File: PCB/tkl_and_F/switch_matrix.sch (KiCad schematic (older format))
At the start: 214 parts

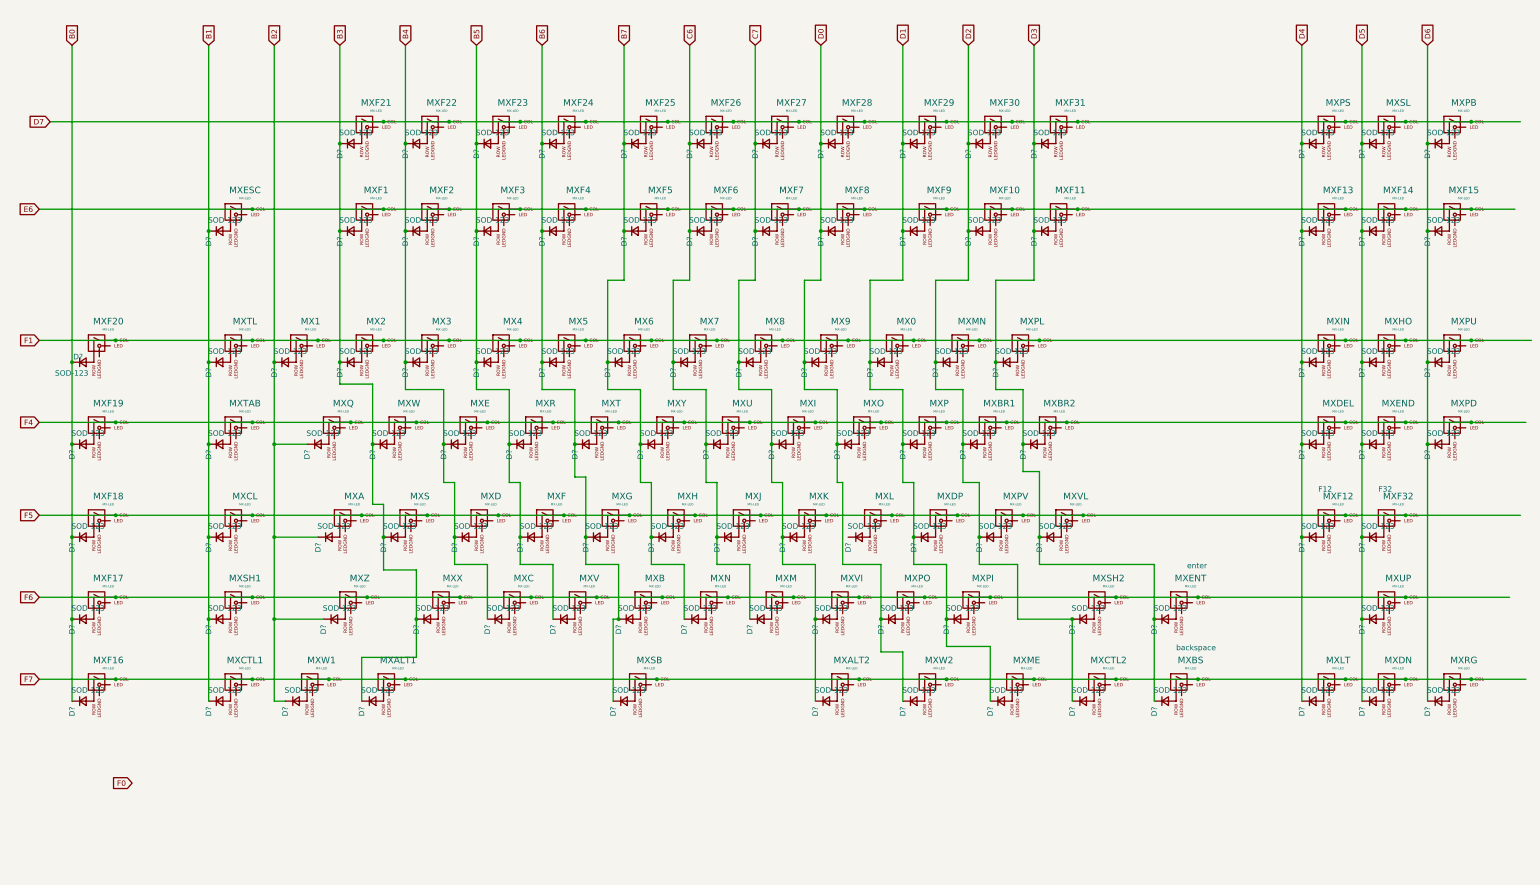
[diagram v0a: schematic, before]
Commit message: footprint assigment
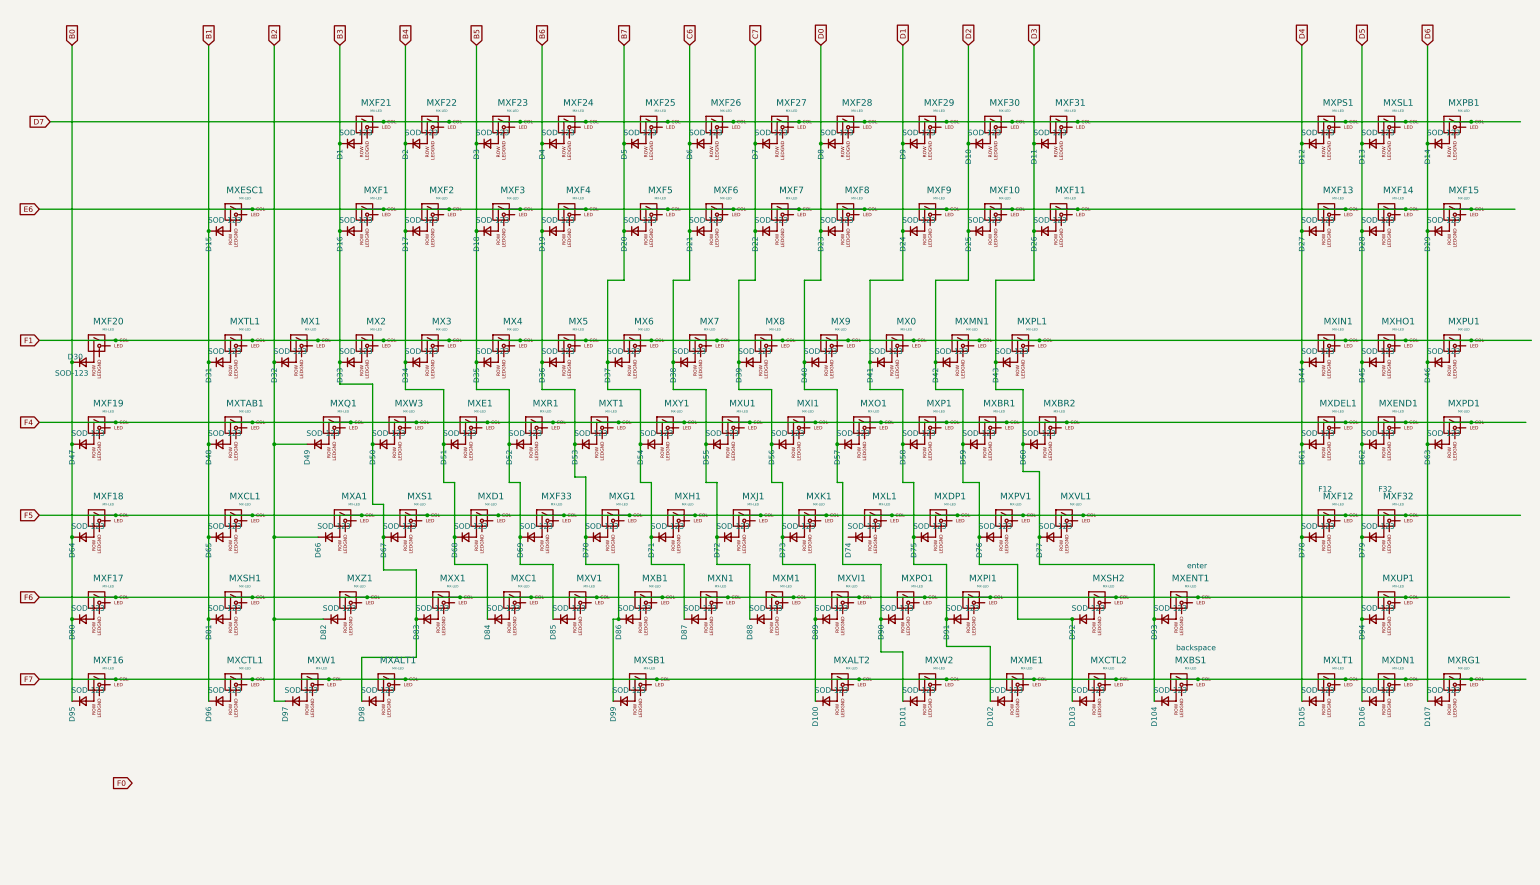
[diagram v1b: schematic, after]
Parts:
- D1, D10, D100, D101, D102, D103, D104, D105, D106, D107, D11, D12, D13, D14, D15, D16, D17, D18, D19, D2, D20, D21, D22, D23, D24, D25, D26, D27, D28, D29, D3, D30, D31, D32, D33, D34, D35, D36, D37, D38, D39, D4, D40, D41, D42, D43, D44, D45, D46, D47, D48, D49, D5, D50, D51, D52, D53, D54, D55, D56, D57, D58, D59, D6, D60, D61, D62, D63, D64, D65, D66, D67, D68, D69, D7, D70, D71, D72, D73, D74, D75, D76, D77, D78, D79, D8, D80, D81, D82, D83, D84, D85, D86, D87, D88, D89, D9, D90, D91, D92, D93, D94, D95, D96, D97, D98, D99: renamed from D?; footprint (none) -> Diodes_SMD:D_SOD-123
- MX0, MX1, MX2, MX3, MX4, MX5, MX6, MX7, MX8, MX9, MXBR1, MXBR2, MXCTL2, MXF1, MXF10, MXF11, MXF12, MXF13, MXF14, MXF15, MXF16, MXF17, MXF18, MXF19, MXF2, MXF20, MXF21, MXF22, MXF23, MXF24, MXF25, MXF26, MXF27, MXF28, MXF29, MXF3, MXF30, MXF31, MXF32, MXF4, MXF5, MXF6, MXF7, MXF8, MXF9: footprint (none) -> MX_Only:MXOnly-1U
- MXA1: renamed from MXA; footprint (none) -> MX_Only:MXOnly-1U
- MXALT1, MXALT2, MXCTL1, MXW1, MXW2: footprint (none) -> MX_Only:MXOnly-1.25U
- MXB1: renamed from MXB; footprint (none) -> MX_Only:MXOnly-1U
- MXBS1: renamed from MXBS; footprint (none) -> MX_Only:MXOnly-2U
- MXC1: renamed from MXC; footprint (none) -> MX_Only:MXOnly-1U
- MXCL1: renamed from MXCL; footprint (none) -> MX_Only:MXOnly-1.75U
- MXD1: renamed from MXD; footprint (none) -> MX_Only:MXOnly-1U
- MXDEL1: renamed from MXDEL; footprint (none) -> MX_Only:MXOnly-1U
- MXDN1: renamed from MXDN; footprint (none) -> MX_Only:MXOnly-1U
- MXDP1: renamed from MXDP; footprint (none) -> MX_Only:MXOnly-1U
- MXE1: renamed from MXE; footprint (none) -> MX_Only:MXOnly-1U
- MXEND1: renamed from MXEND; footprint (none) -> MX_Only:MXOnly-1U
- MXENT1: renamed from MXENT; footprint (none) -> MX_Only:MXOnly-1U
- MXESC1: renamed from MXESC; footprint (none) -> MX_Only:MXOnly-1U
- MXF33: renamed from MXF; footprint (none) -> MX_Only:MXOnly-1U
- MXG1: renamed from MXG; footprint (none) -> MX_Only:MXOnly-1U
- MXH1: renamed from MXH; footprint (none) -> MX_Only:MXOnly-1U
- MXHO1: renamed from MXHO; footprint (none) -> MX_Only:MXOnly-1U
- MXI1: renamed from MXI; footprint (none) -> MX_Only:MXOnly-1U
- MXIN1: renamed from MXIN; footprint (none) -> MX_Only:MXOnly-1U
- MXJ1: renamed from MXJ; footprint (none) -> MX_Only:MXOnly-1U
- MXK1: renamed from MXK; footprint (none) -> MX_Only:MXOnly-1U
- MXL1: renamed from MXL; footprint (none) -> MX_Only:MXOnly-1U
- MXLT1: renamed from MXLT; footprint (none) -> MX_Only:MXOnly-1U
- MXM1: renamed from MXM; footprint (none) -> MX_Only:MXOnly-1U
- MXME1: renamed from MXME; footprint (none) -> MX_Only:MXOnly-1.25U
- MXMN1: renamed from MXMN; footprint (none) -> MX_Only:MXOnly-1U
- MXN1: renamed from MXN; footprint (none) -> MX_Only:MXOnly-1U
- MXO1: renamed from MXO; footprint (none) -> MX_Only:MXOnly-1U
- MXP1: renamed from MXP; footprint (none) -> MX_Only:MXOnly-1U
- MXPB1: renamed from MXPB; footprint (none) -> MX_Only:MXOnly-1U
- MXPD1: renamed from MXPD; footprint (none) -> MX_Only:MXOnly-1U
- MXPI1: renamed from MXPI; footprint (none) -> MX_Only:MXOnly-1U
- MXPL1: renamed from MXPL; footprint (none) -> MX_Only:MXOnly-1U
- MXPO1: renamed from MXPO; footprint (none) -> MX_Only:MXOnly-1U
- MXPS1: renamed from MXPS; footprint (none) -> MX_Only:MXOnly-1U
- MXPU1: renamed from MXPU; footprint (none) -> MX_Only:MXOnly-1U
- MXPV1: renamed from MXPV; footprint (none) -> MX_Only:MXOnly-1U
- MXQ1: renamed from MXQ; footprint (none) -> MX_Only:MXOnly-1U
- MXR1: renamed from MXR; footprint (none) -> MX_Only:MXOnly-1U
- MXRG1: renamed from MXRG; footprint (none) -> MX_Only:MXOnly-1U
- MXS1: renamed from MXS; footprint (none) -> MX_Only:MXOnly-1U
- MXSB1: renamed from MXSB; footprint (none) -> MX_Only:MXOnly-6.25U
- MXSH1: footprint (none) -> MX_Only:MXOnly-2.25U
- MXSH2: footprint (none) -> MX_Only:MXOnly-2.75U
- MXSL1: renamed from MXSL; footprint (none) -> MX_Only:MXOnly-1U
- MXT1: renamed from MXT; footprint (none) -> MX_Only:MXOnly-1U
- MXTAB1: renamed from MXTAB; footprint (none) -> MX_Only:MXOnly-1.5U
- MXTL1: renamed from MXTL; footprint (none) -> MX_Only:MXOnly-1U
- MXU1: renamed from MXU; footprint (none) -> MX_Only:MXOnly-1U
- MXUP1: renamed from MXUP; footprint (none) -> MX_Only:MXOnly-1U
- MXV1: renamed from MXV; footprint (none) -> MX_Only:MXOnly-1U
- MXVI1: renamed from MXVI; footprint (none) -> MX_Only:MXOnly-1U
- MXVL1: renamed from MXVL; footprint (none) -> MX_Only:MXOnly-1U
- MXW3: renamed from MXW; footprint (none) -> MX_Only:MXOnly-1U
- MXX1: renamed from MXX; footprint (none) -> MX_Only:MXOnly-1U
- MXY1: renamed from MXY; footprint (none) -> MX_Only:MXOnly-1U
- MXZ1: renamed from MXZ; footprint (none) -> MX_Only:MXOnly-1U

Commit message: avancement
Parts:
- MXENT1: footprint MX_Only:MXOnly-1U -> MX_Only:MXOnly-ISO
- renumbered MXPV1 to MXQM1
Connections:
- wire segments 312 -> 324
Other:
- moved on the sheet: D1, D10, D100, D101, D102, D103, D104, D105, D106, D107, D11, D12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
